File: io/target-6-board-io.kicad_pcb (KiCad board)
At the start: 2 copper layers, 99.1 x 90.7 mm, 55 parts, among them J1 Conn_01x10_Socket, J10 RJ14, J11 RJ14, J12 RJ14, J13 RJ14, J14 USB_A, J15 USB_A, J16 USB_C_Receptacle_PowerOnly_6P, J2 Conn_01x12_Socket, J3 Conn_01x10_Socket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

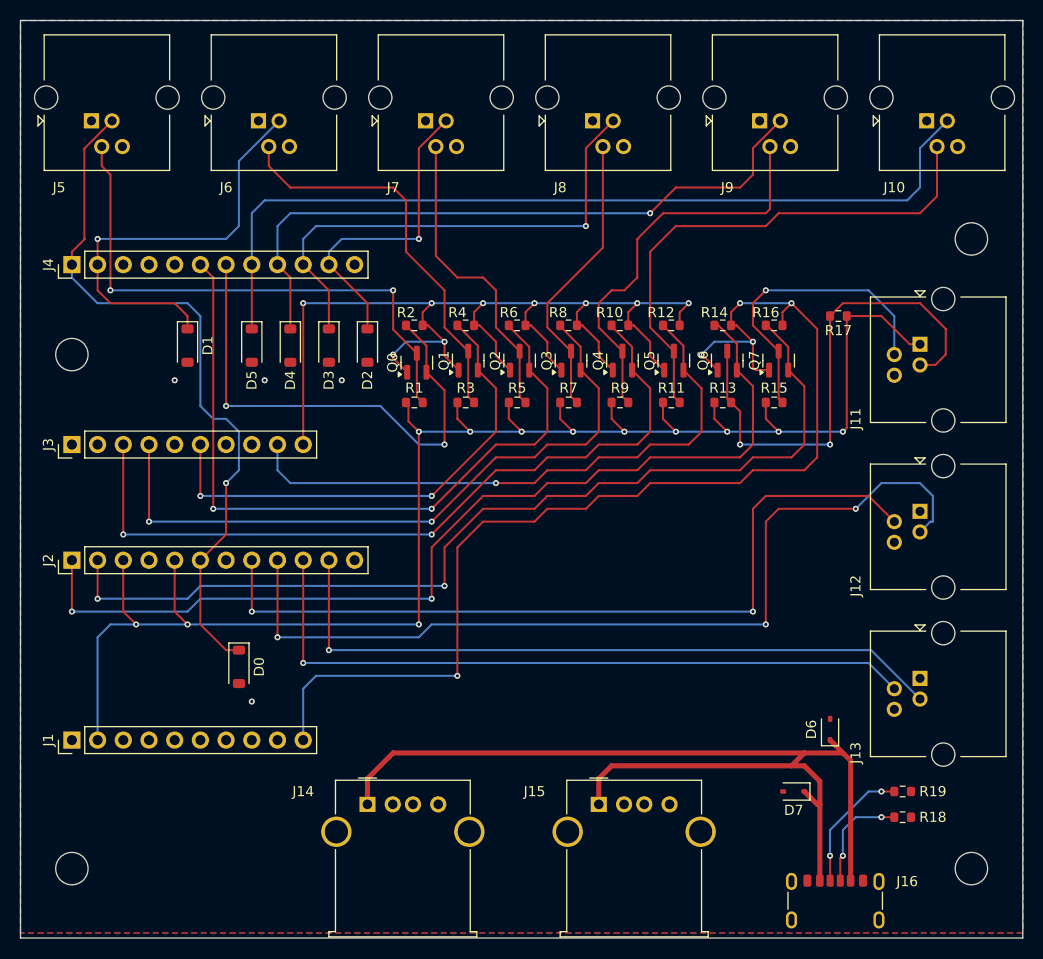
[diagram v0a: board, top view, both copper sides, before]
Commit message: io: shrink board edge and move mounting holes, pin headers
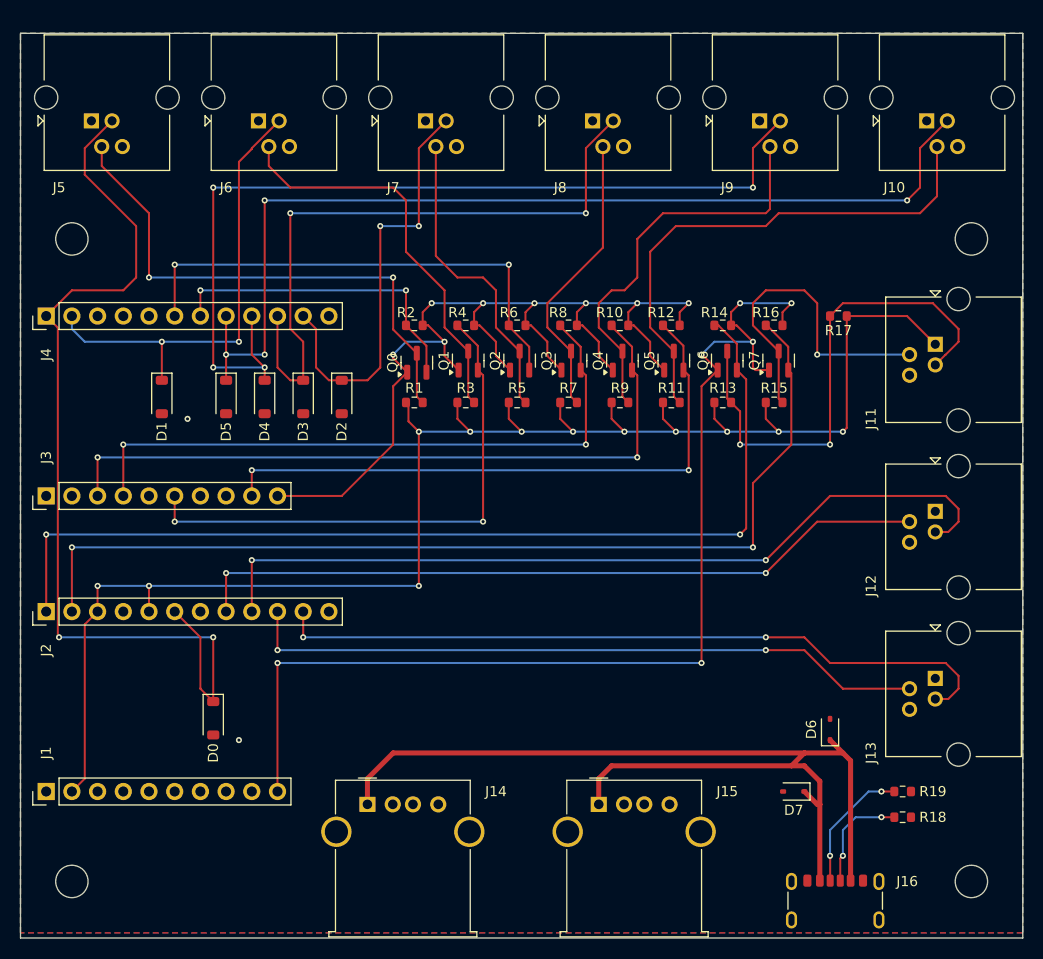
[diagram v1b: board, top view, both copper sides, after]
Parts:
- moved H3 11.4 mm to (30.5, 47.0)
- moved D0 5.68 mm to (44.5, 94.4)
- moved D1 5.68 mm to (39.4, 62.6)
- moved D2 5.68 mm to (57.1, 62.6)
- moved D3 5.68 mm to (53.3, 62.6)
- moved D4 5.68 mm to (49.5, 62.6)
- moved D5 5.68 mm to (45.7, 62.6)
- moved J1 5.68 mm to (27.9, 101.6)
- moved J2 5.68 mm to (27.9, 83.8)
- moved J3 5.68 mm to (27.9, 72.4)
- moved J4 5.68 mm to (27.9, 54.6)
- moved J11 1.51 mm to (115.8, 57.4)
- moved J12 1.51 mm to (115.8, 73.9)
- moved J13 1.51 mm to (115.8, 90.4)
- moved H1 1.27 mm to (30.5, 110.5)
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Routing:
- net S0_GPIO6: track 66.2 -> 90.8 mm, vias 1 -> 4
- net S0_GPIO10: track 72.5 -> 49.4 mm
- net C_GPIO10: track 70.7 -> 93.5 mm, vias 1 -> 2
- net S0_GPIO8: track 50.1 -> 31.8 mm
- net S0_GPIO5: track 49.9 -> 64.6 mm, vias 1 -> 2
- net S0_GPIO7: track 86.2 -> 98.4 mm, vias 0 -> 4
- net S0_GPIO4: track 31.4 -> 42.3 mm, vias 1 -> 2
- net CHIGH_IN: track 89.4 -> 82.1 mm, vias 3 -> 2
- net CHIGH_OUT: track 80.3 -> 73.5 mm
- net S0_GPIO19: track 77.3 -> 71.3 mm
- net S0_VCC3V3: track 106.0 -> 100.6 mm, vias 9 -> 8
- net S0_GPIO9: track 48.6 -> 53.5 mm
- net C_VCC3V3: track 114.2 -> 109.3 mm, vias 5 -> 6
- net S0_GPIO18: track 67.4 -> 63.6 mm
- net CLOW_IN: track 69.3 -> 72.9 mm, vias 1 -> 2
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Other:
- board size 99.1 x 90.7 mm -> 99.1 x 89.4 mm

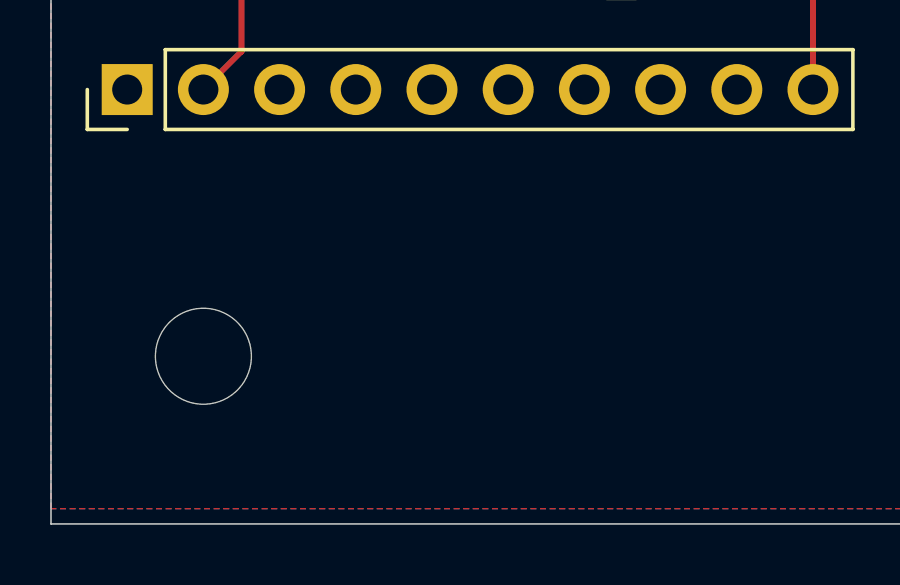
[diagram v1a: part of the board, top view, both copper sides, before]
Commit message: io: add board name and version
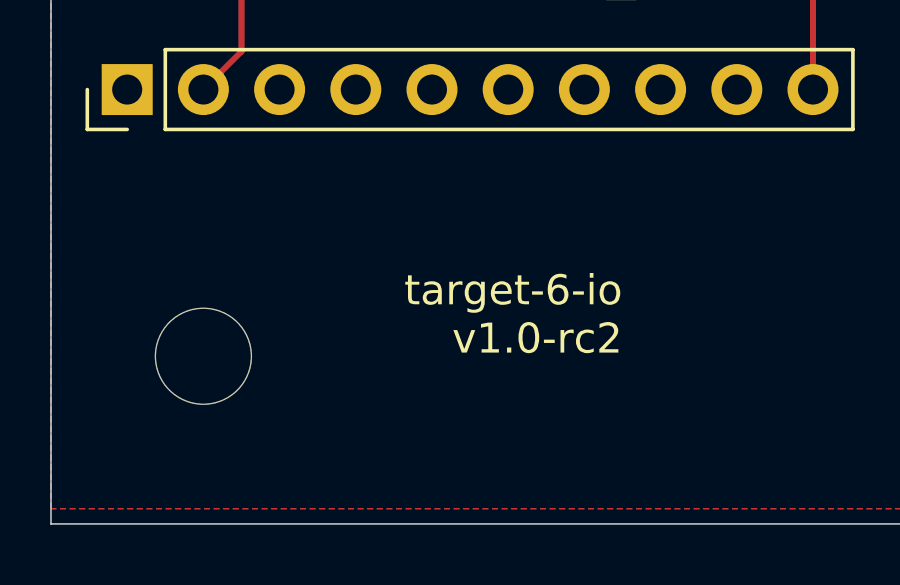
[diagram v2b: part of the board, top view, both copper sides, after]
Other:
- board text added: "target-6-io v1.0-rc2"
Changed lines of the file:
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@@
   (gr_rect (start 25.4 26.67) (end 124.46 116.08)
     (stroke (width 0.05) (type default)) (fill none) (layer "Edge.Cuts"))
+  (gr_text "target-6-io\nv1.0-rc2" (at 44.45 110.49) (layer "F.SilkS")
+    (effects (font (size 1 1) (thickness 0.1)) (justify right bottom))
+  )
   (via (at 41.91 64.77) (size 0.6) (drill 0.3) (layers "F.Cu" "B.Cu") (free) (net 1))
   (via (at 46.99 96.52) (size 0.6) (drill 0.3) (layers "F.Cu" "B.Cu") (free) (net 1))
